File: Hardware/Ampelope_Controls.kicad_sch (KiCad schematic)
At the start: 36 parts, among them J1 Conn_01x12_Male, J10 Audio2_In, J11 Audio3_In, J12 Audio4_In, J13 Audio1_Out, J14 Audio2_Out, J15 Audio3_Out, J16 Audio4_Out, J17 Clock_In, J18 Env1_Out, J19 Env3_Out, J2 Conn_01x12_Male, J3 Conn_01x12_Male, J4 Conn_01x12_Male, J5 Gate1_In, J6 Gate2_In, J7 Gate3_In, J8 Gate4_In, J9 Audio1_In

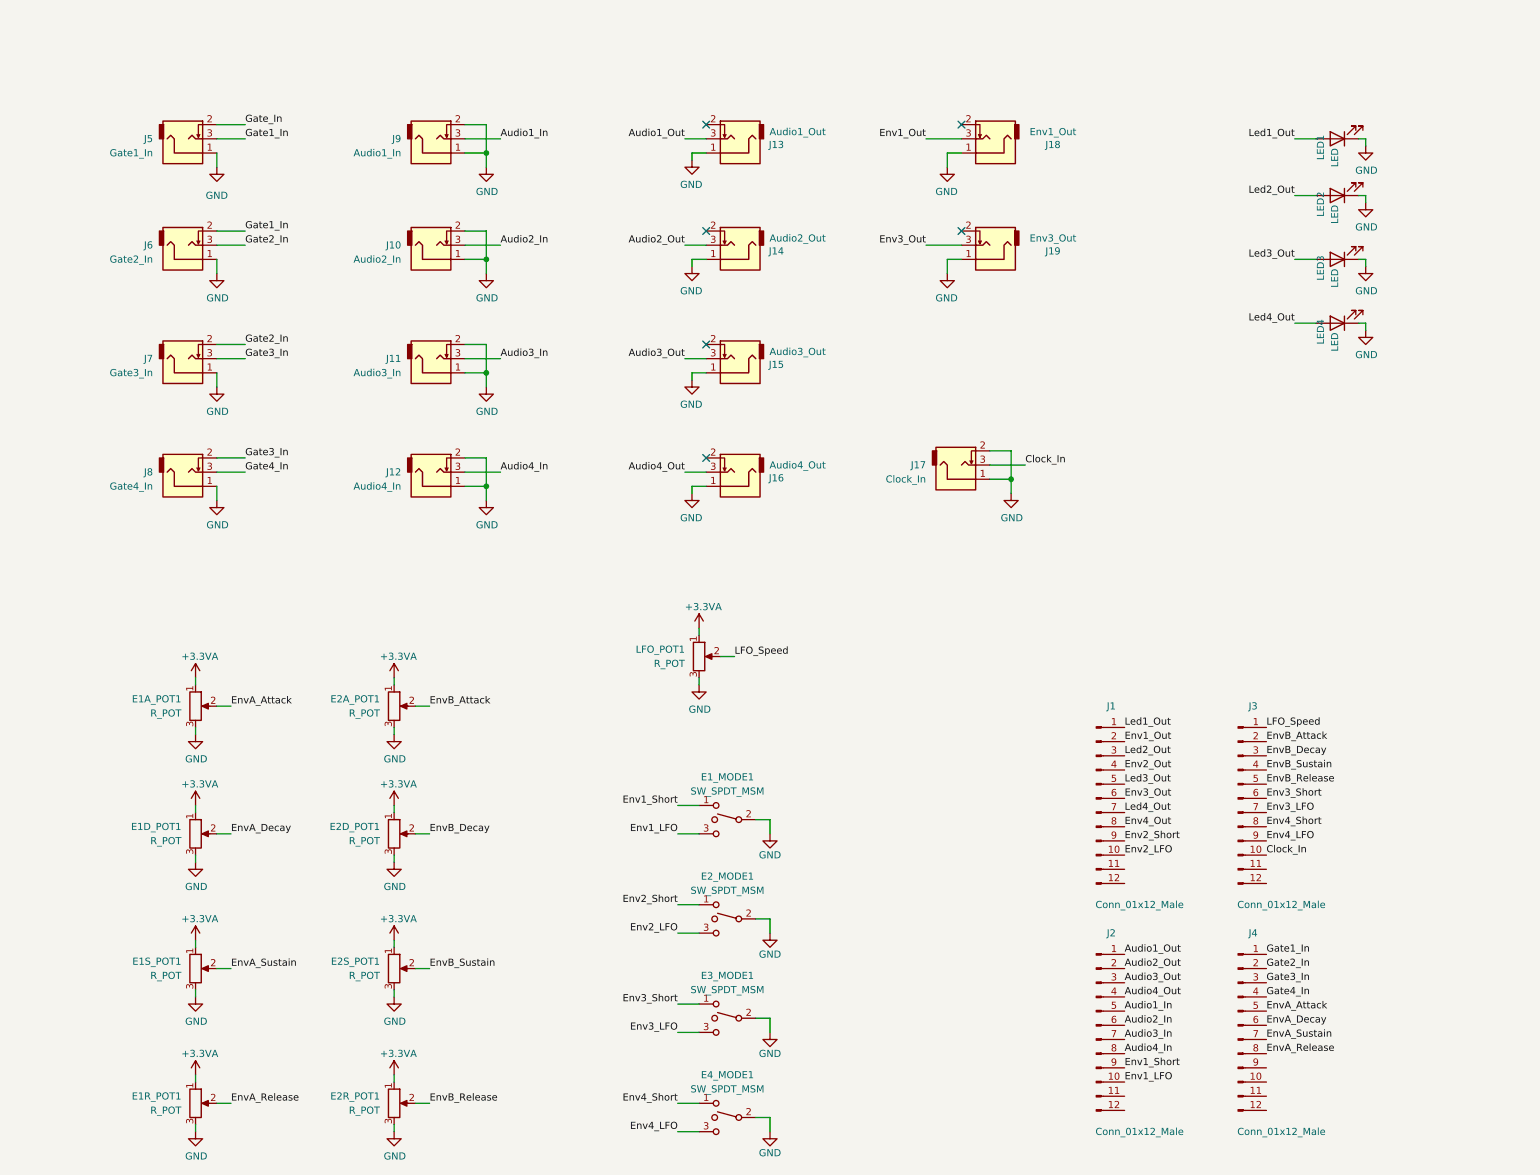
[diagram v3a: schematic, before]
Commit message: Added test points to component PCB; Added 3D mockups
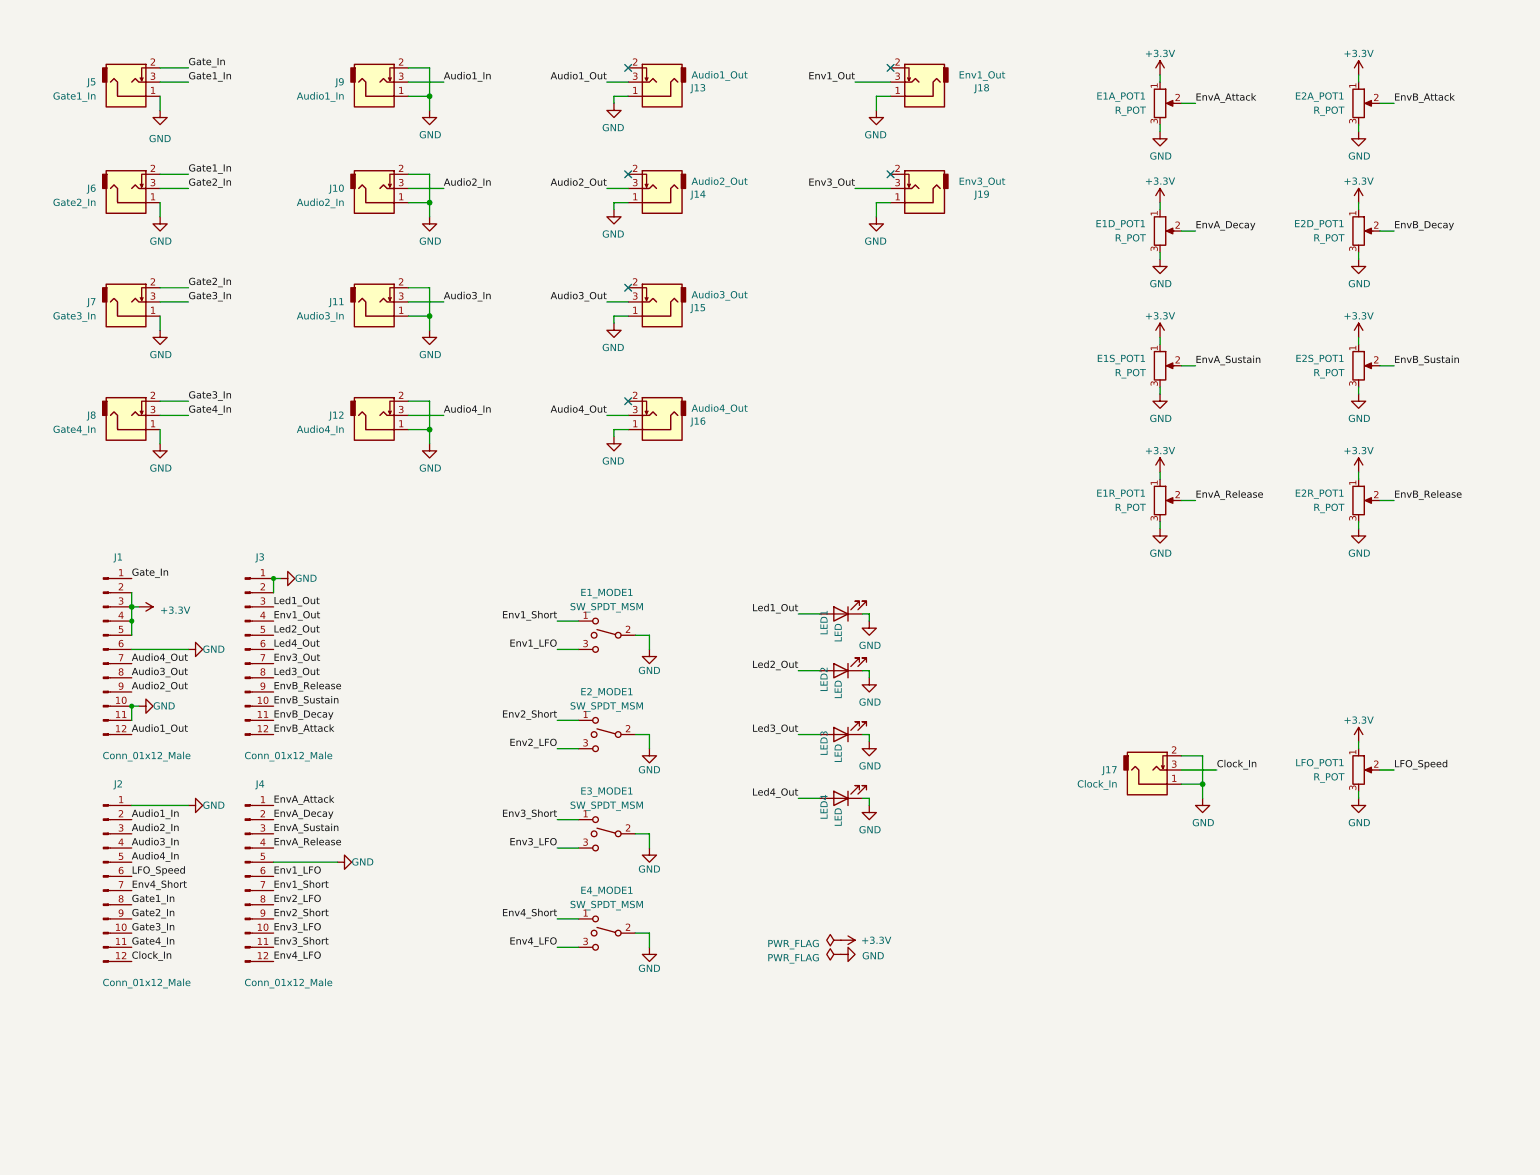
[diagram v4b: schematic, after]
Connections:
- net Env2_Out is gone; now on net +3V3: J1.4 (Pin_4)
- net Env4_Out is gone; now on net Audio3_Out: J1.8 (Pin_8)
- net Audio1_In: now also J2.2 (Pin_2); no longer J2.5 (Pin_5)
- net Audio1_Out: now also J1.12 (Pin_12); no longer J2.1 (Pin_1)
- net Audio2_In: now also J2.3 (Pin_3); no longer J2.6 (Pin_6)
- net Audio2_Out: now also J1.9 (Pin_9); no longer J2.2 (Pin_2)
- net Audio3_In: now also J2.4 (Pin_4); no longer J2.7 (Pin_7)
- net Audio3_Out: no longer J2.3 (Pin_3)
- net Audio4_In: now also J2.5 (Pin_5); no longer J2.8 (Pin_8)
- net Audio4_Out: now also J1.7 (Pin_7); no longer J2.4 (Pin_4)
- net Clock_In: now also J2.12 (Pin_12); no longer J3.10 (Pin_10)
- net Env1_LFO: now also J4.6 (Pin_6); no longer J2.10 (Pin_10)
- net Env1_Out: now also J3.4 (Pin_4); no longer J1.2 (Pin_2)
- net Env1_Short: now also J4.7 (Pin_7); no longer J2.9 (Pin_9)
- net Env2_LFO: now also J4.8 (Pin_8); no longer J1.10 (Pin_10)
- net Env2_Short: now also J4.9 (Pin_9); no longer J1.9 (Pin_9)
- net Env3_LFO: now also J4.10 (Pin_10); no longer J3.7 (Pin_7)
- net Env3_Out: now also J3.7 (Pin_7); no longer J1.6 (Pin_6)
- net Env3_Short: now also J4.11 (Pin_11); no longer J3.6 (Pin_6)
- net Env4_LFO: now also J4.12 (Pin_12); no longer J3.9 (Pin_9)
- net Env4_Short: now also J2.7 (Pin_7); no longer J3.8 (Pin_8)
- net EnvA_Attack: now also J4.1 (Pin_1); no longer J4.5 (Pin_5)
- net EnvA_Decay: now also J4.2 (Pin_2); no longer J4.6 (Pin_6)
- net EnvA_Release: now also J4.4 (Pin_4); no longer J4.8 (Pin_8)
- net EnvA_Sustain: now also J4.3 (Pin_3); no longer J4.7 (Pin_7)
- net EnvB_Attack: now also J3.12 (Pin_12); no longer J3.2 (Pin_2)
- net EnvB_Decay: now also J3.11 (Pin_11); no longer J3.3 (Pin_3)
- net EnvB_Release: now also J3.9 (Pin_9); no longer J3.5 (Pin_5)
- net EnvB_Sustain: now also J3.10 (Pin_10); no longer J3.4 (Pin_4)
- net GND: now also J1.10 (Pin_10), J1.11 (Pin_11), J1.6 (Pin_6), J2.1 (Pin_1), J3.1 (Pin_1), J3.2 (Pin_2), J4.5 (Pin_5)
- net Gate1_In: now also J2.8 (Pin_8); no longer J4.1 (Pin_1)
- net Gate2_In: now also J2.9 (Pin_9); no longer J4.2 (Pin_2)
- net Gate3_In: now also J2.10 (Pin_10); no longer J4.3 (Pin_3)
- net Gate4_In: now also J2.11 (Pin_11); no longer J4.4 (Pin_4)
- net Gate_In: now also J1.1 (Pin_1)
- net LFO_Speed: now also J2.6 (Pin_6); no longer J3.1 (Pin_1)
- net Led1_Out: now also J3.3 (Pin_3); no longer J1.1 (Pin_1)
- net Led2_Out: now also J3.5 (Pin_5); no longer J1.3 (Pin_3)
- net Led3_Out: now also J3.8 (Pin_8); no longer J1.5 (Pin_5)
- net Led4_Out: now also J3.6 (Pin_6); no longer J1.7 (Pin_7)
- net +3.3VA renamed +3V3
- net +3V3: now also J1.2 (Pin_2), J1.3 (Pin_3), J1.5 (Pin_5)
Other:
- moved on the sheet: E1A_POT1, E1D_POT1, E1R_POT1, E1S_POT1, E1_MODE1, E2A_POT1, E2D_POT1, E2R_POT1, E2S_POT1, E2_MODE1, E3_MODE1, E4_MODE1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

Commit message: Fixed DRC errors on control and component boards
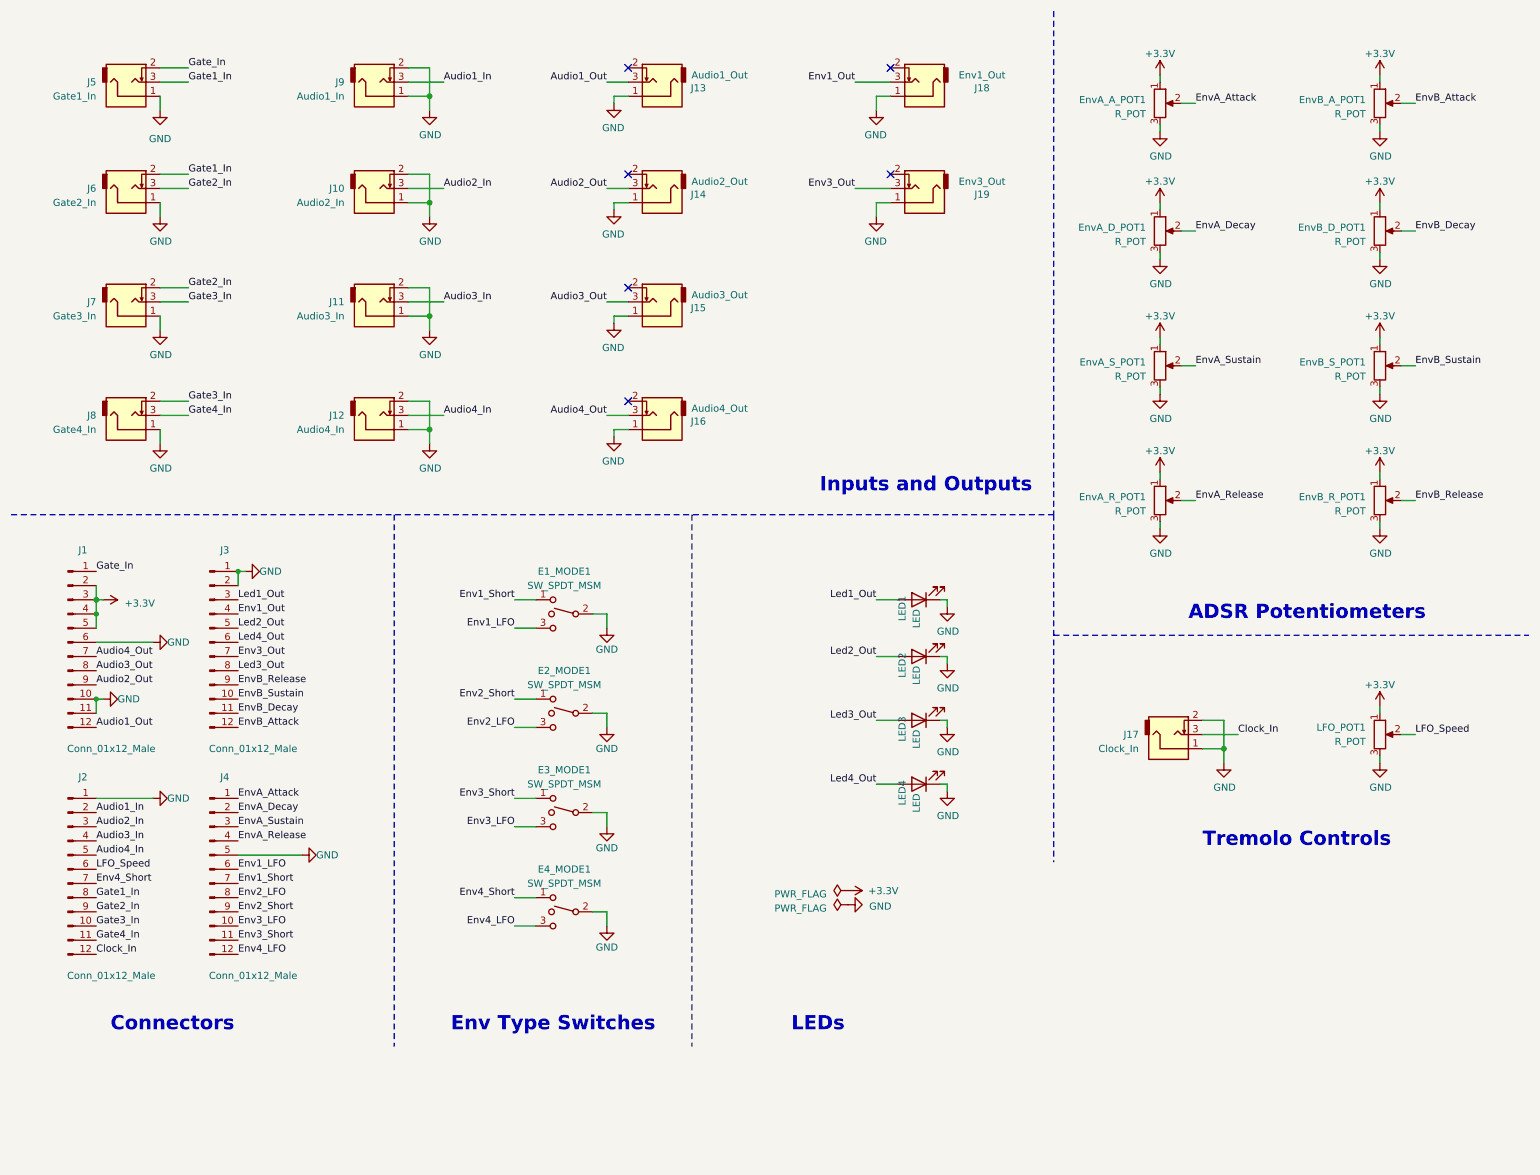
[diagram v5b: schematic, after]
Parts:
- renumbered E1A_POT1 to EnvA_A_POT1, E1D_POT1 to EnvA_D_POT1, E1R_POT1 to EnvA_R_POT1, E1S_POT1 to EnvA_S_POT1, E2A_POT1 to EnvB_A_POT1, E2D_POT1 to EnvB_D_POT1, E2R_POT1 to EnvB_R_POT1, E2S_POT1 to EnvB_S_POT1
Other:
- note added: "ADSR Potentiometers"
- note added: "Connectors"
- note added: "Env Type Switches"
- note added: "Inputs and Outputs"
- note added: "LEDs"
- note added: "Tremolo Controls"
- moved on the sheet: E1_MODE1, E2_MODE1, E3_MODE1, E4_MODE1, EnvB_A_POT1, EnvB_D_POT1, EnvB_R_POT1, EnvB_S_POT1, J1, J17, J2, J3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

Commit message: Various schematic and PCB tidying
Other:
- company: (none) -> Mountjoy Modular
- title: (none) -> Ampelope Controls Board
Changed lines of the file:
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@@
-(kicad_sch (version 20210615) (generator eeschema)
+(kicad_sch (version 20210621) (generator eeschema)
   (paper "A4")
+  (title_block
+    (title "Ampelope Controls Board")
+    (company "Mountjoy Modular")
+  )
   (junction (at 27.94 118.11) (diameter 1.016) (color 0 0 0 0))
   (junction (at 27.94 120.65) (diameter 0.9144) (color 0 0 0 0))
